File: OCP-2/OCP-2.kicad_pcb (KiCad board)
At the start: 2 copper layers, 100 x 100 mm, 139 parts, among them X1 ico*отверстие*М3, X2 ico*отверстие*М3

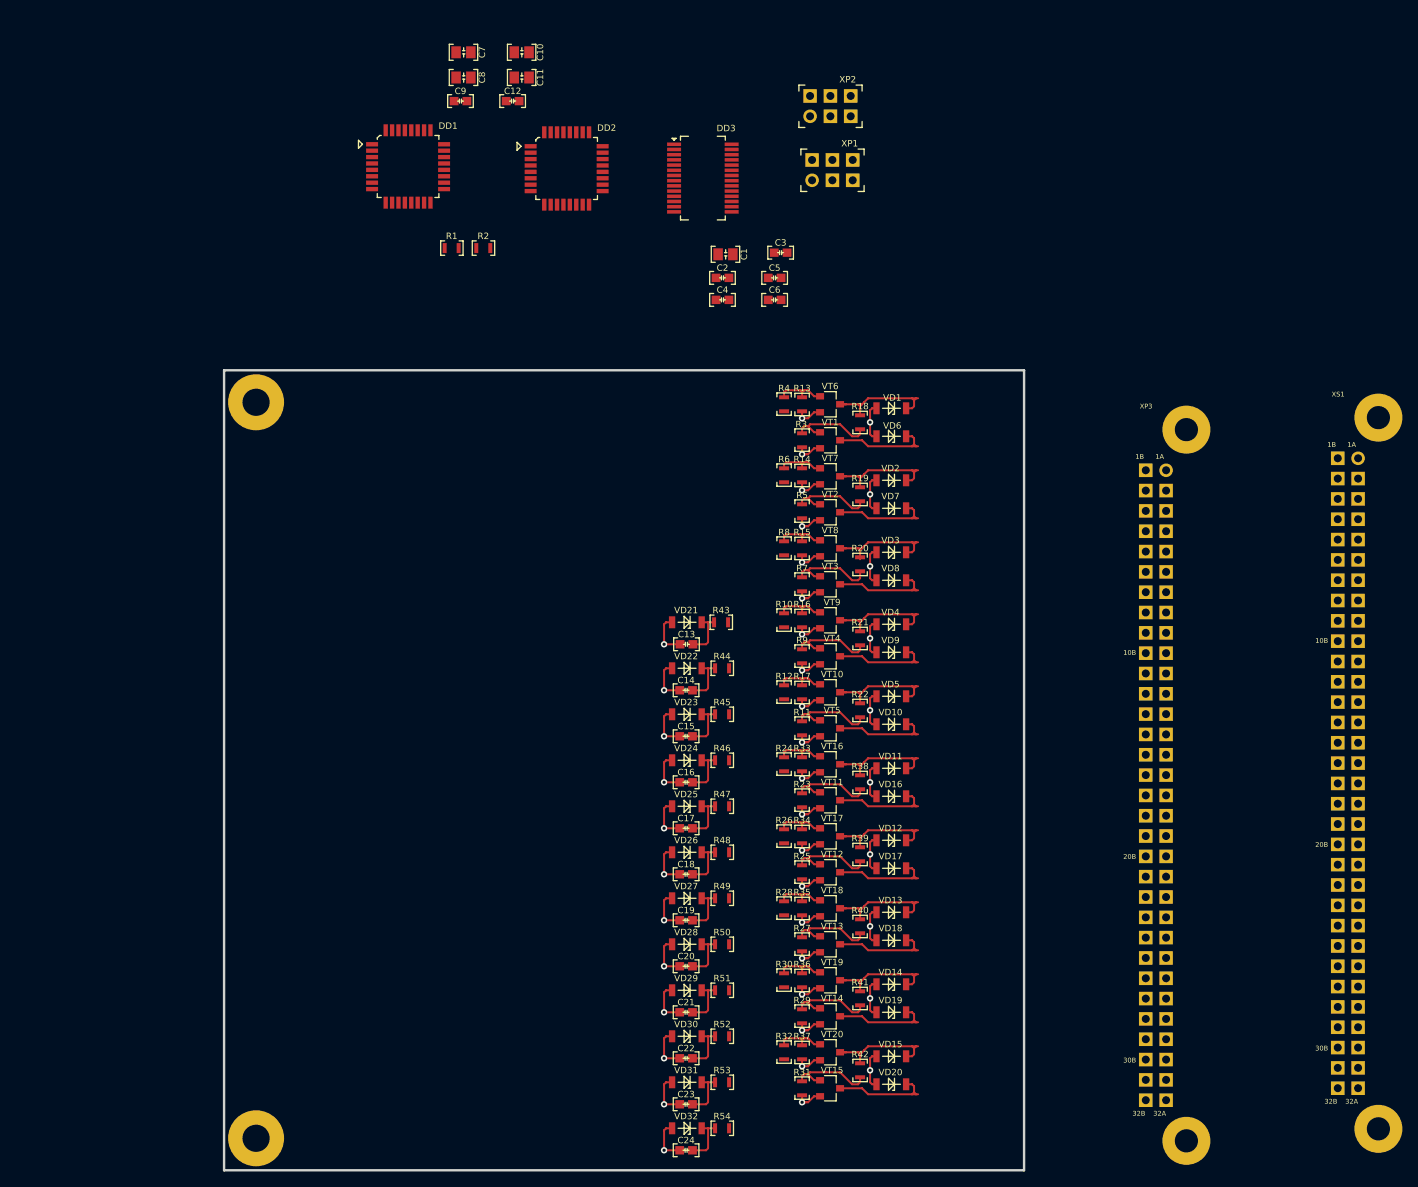
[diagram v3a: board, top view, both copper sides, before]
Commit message: размещена схема DI, схема не подбита
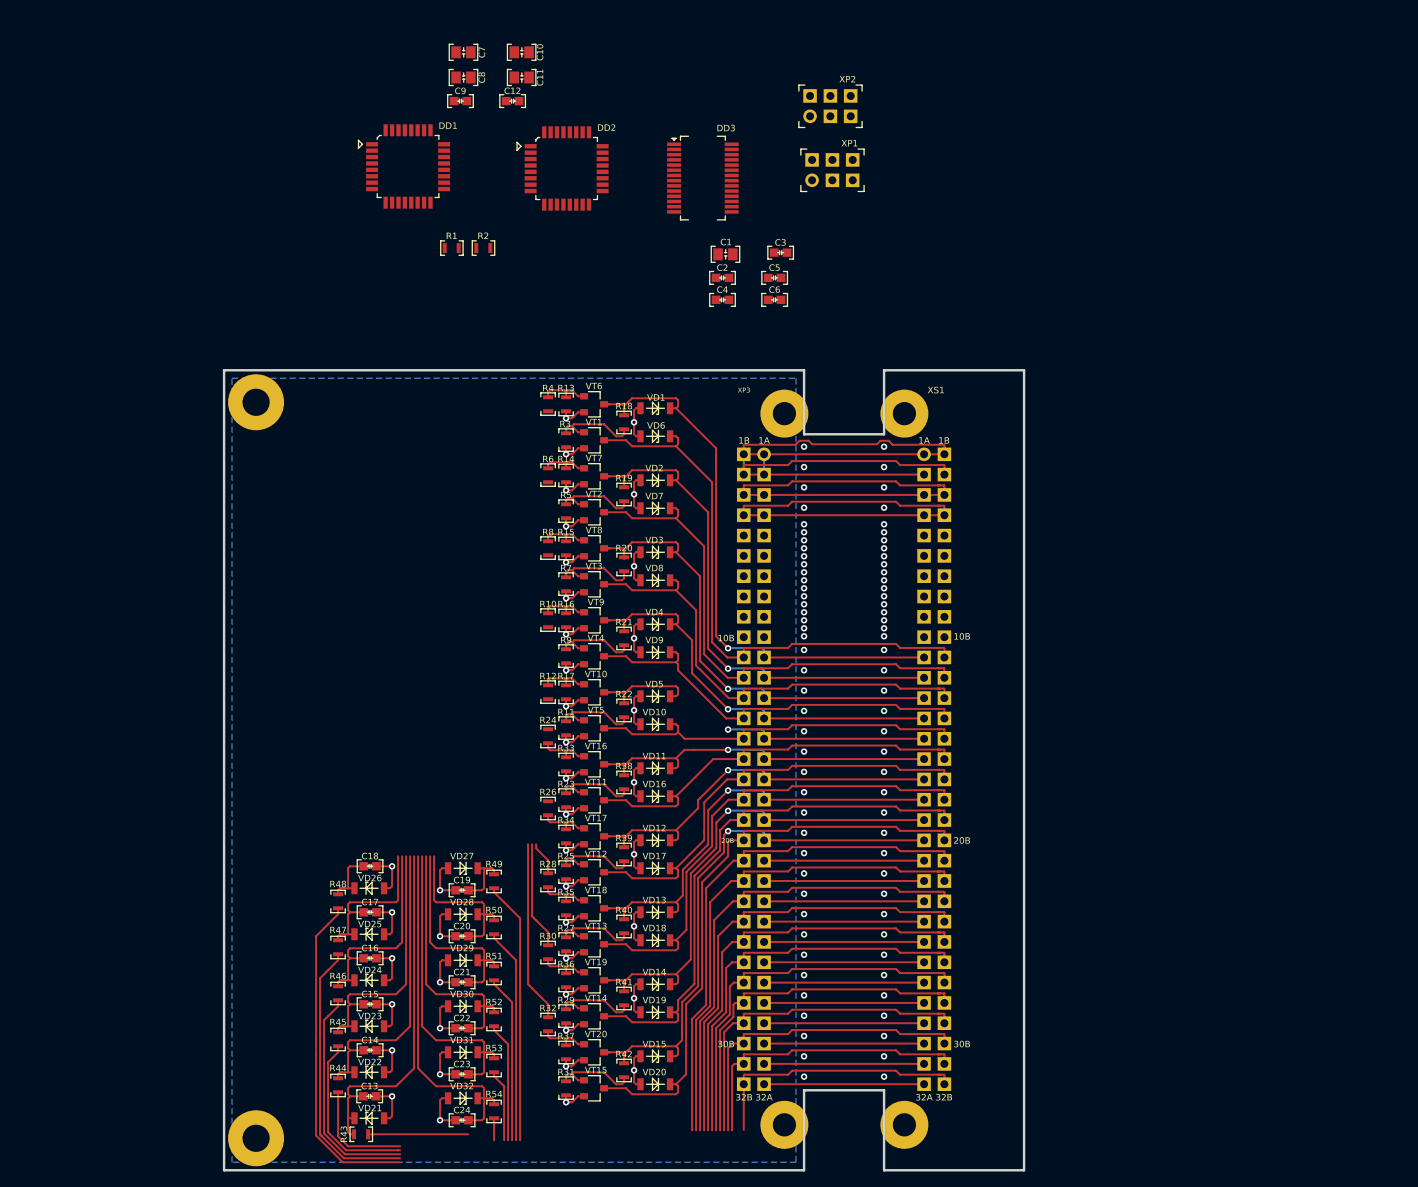
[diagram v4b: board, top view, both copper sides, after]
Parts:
- moved R43 78.2 mm to (67.1, 145.5)
- moved VD21 71.7 mm to (70.0, 143.5), turned to 180 degrees
- moved R44 70.9 mm to (64.2, 139.4), turned to 270 degrees
- moved C13 69.0 mm to (68.2, 140.8), turned to 180 degrees
- moved R45 62.9 mm to (64.2, 133.6), turned to 270 degrees
- moved VD22 62.0 mm to (70.0, 137.8), turned to 180 degrees
- moved C14 59.9 mm to (68.2, 135.0), turned to 180 degrees
- moved R46 56.1 mm to (64.2, 127.9), turned to 270 degrees
- moved XS1 54.3 mm to (137.5, 60.5)
- moved VD23 53.1 mm to (70.0, 132.0), turned to 180 degrees
- moved C15 51.8 mm to (68.2, 129.2), turned to 180 degrees
- moved R47 51.1 mm to (64.2, 122.1), turned to 270 degrees
- moved XP3 50.3 mm to (117.5, 60.5)
- moved R48 48.4 mm to (64.2, 116.4), turned to 270 degrees
- moved VD24 45.3 mm to (70.0, 126.2), turned to 180 degrees
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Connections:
- VD10 pad 2: /DOU5.PNP -> /DOUT5.PNP
- VD20 pad 2: /DOU10.PNP -> /DOUT10.PNP
- VT15 pad 3: /DOU10.PNP -> /DOUT10.PNP
- VT5 pad 3: /DOU5.PNP -> /DOUT5.PNP
- XP3 pad 11A: Net-(XP3-Pad11A) -> /DOUT1.NPN
- XP3 pad 11B: Net-(XP3-Pad11B) -> /DOUT1.PNP
- XP3 pad 12A: Net-(XP3-Pad12A) -> /DOUT2.NPN
- XP3 pad 12B: Net-(XP3-Pad12B) -> /DOUT2.PNP
- XP3 pad 13A: Net-(XP3-Pad13A) -> /DOUT3.NPN
- XP3 pad 13B: Net-(XP3-Pad13B) -> /DOUT3.PNP
- XP3 pad 14A: Net-(XP3-Pad14A) -> /DOUT4.NPN
- XP3 pad 14B: Net-(XP3-Pad14B) -> /DOUT4.PNP
- XP3 pad 15A: Net-(XP3-Pad15A) -> /DOUT5.NPN
- XP3 pad 15B: Net-(XP3-Pad15B) -> /DOUT5.PNP
- XP3 pad 16A: Net-(XP3-Pad16A) -> /DOUT6.NPN
- XP3 pad 16B: Net-(XP3-Pad16B) -> /DOUT6.PNP
- XP3 pad 17A: Net-(XP3-Pad17A) -> /DOUT7.NPN
- XP3 pad 17B: Net-(XP3-Pad17B) -> /DOUT7.PNP
- XP3 pad 18A: Net-(XP3-Pad18A) -> /DOUT8.NPN
- XP3 pad 18B: Net-(XP3-Pad18B) -> /DOUT8.PNP
- XP3 pad 19A: Net-(XP3-Pad19A) -> /DOUT9.NPN
- XP3 pad 19B: Net-(XP3-Pad19B) -> /DOUT9.PNP
- XP3 pad 1A: Net-(XP3-Pad1A) -> 5V
- XP3 pad 1B: Net-(XP3-Pad1B) -> 5V
- XP3 pad 20A: Net-(XP3-Pad20A) -> /DOUT10.NPN
- XP3 pad 20B: Net-(XP3-Pad20B) -> /DOUT10.PNP
- XP3 pad 21A: Net-(XP3-Pad21A) -> /RESERVE1
- XP3 pad 21B: Net-(XP3-Pad21B) -> /DIN1
- XP3 pad 22A: Net-(XP3-Pad22A) -> /RESERVE2
- XP3 pad 22B: Net-(XP3-Pad22B) -> /DIN2
- XP3 pad 23A: Net-(XP3-Pad23A) -> /RESERVE3
- XP3 pad 23B: Net-(XP3-Pad23B) -> /DIN3
- XP3 pad 24A: Net-(XP3-Pad24A) -> /RESERVE4
- XP3 pad 24B: Net-(XP3-Pad24B) -> /DIN4
- XP3 pad 25A: Net-(XP3-Pad25A) -> /RESERVE5
- XP3 pad 25B: Net-(XP3-Pad25B) -> /DIN5
- XP3 pad 26A: Net-(XP3-Pad26A) -> /RESERVE6
- XP3 pad 26B: Net-(XP3-Pad26B) -> /DIN6
- XP3 pad 27A: Net-(XP3-Pad27A) -> /RESERVE7
- XP3 pad 27B: Net-(XP3-Pad27B) -> /DIN7
- XP3 pad 28A: Net-(XP3-Pad28A) -> /RESERVE8
- XP3 pad 28B: Net-(XP3-Pad28B) -> /DIN8
- XP3 pad 29A: Net-(XP3-Pad29A) -> /RESERVE9
- XP3 pad 29B: Net-(XP3-Pad29B) -> /DIN9
- XP3 pad 2A: Net-(XP3-Pad2A) -> 5V
- XP3 pad 2B: Net-(XP3-Pad2B) -> 5V
- XP3 pad 30A: Net-(XP3-Pad30A) -> /RESERVE10
- XP3 pad 30B: Net-(XP3-Pad30B) -> /DIN10
- XP3 pad 31A: Net-(XP3-Pad31A) -> /RESERVE11
- XP3 pad 31B: Net-(XP3-Pad31B) -> /DIN11
- XP3 pad 32A: Net-(XP3-Pad32A) -> /RESERVE12
- XP3 pad 32B: Net-(XP3-Pad32B) -> /DIN12
- XP3 pad 3A: Net-(XP3-Pad3A) -> GND
- XP3 pad 3B: Net-(XP3-Pad3B) -> GND
- XP3 pad 4A: Net-(XP3-Pad4A) -> GND
- XP3 pad 4B: Net-(XP3-Pad4B) -> GND
- XS1 pad 11A: Net-(XS1-Pad11A) -> /DOUT1.NPN
- XS1 pad 11B: Net-(XS1-Pad11B) -> /DOUT1.PNP
- XS1 pad 12A: Net-(XS1-Pad12A) -> /DOUT2.NPN
- XS1 pad 12B: Net-(XS1-Pad12B) -> /DOUT2.PNP
- XS1 pad 13A: Net-(XS1-Pad13A) -> /DOUT3.NPN
- XS1 pad 13B: Net-(XS1-Pad13B) -> /DOUT3.PNP
- XS1 pad 14A: Net-(XS1-Pad14A) -> /DOUT4.NPN
- XS1 pad 14B: Net-(XS1-Pad14B) -> /DOUT4.PNP
- XS1 pad 15A: Net-(XS1-Pad15A) -> /DOUT5.NPN
- XS1 pad 15B: Net-(XS1-Pad15B) -> /DOUT5.PNP
- XS1 pad 16A: Net-(XS1-Pad16A) -> /DOUT6.NPN
- XS1 pad 16B: Net-(XS1-Pad16B) -> /DOUT6.PNP
- XS1 pad 17A: Net-(XS1-Pad17A) -> /DOUT7.NPN
- XS1 pad 17B: Net-(XS1-Pad17B) -> /DOUT7.PNP
- XS1 pad 18A: Net-(XS1-Pad18A) -> /DOUT8.NPN
- XS1 pad 18B: Net-(XS1-Pad18B) -> /DOUT8.PNP
- XS1 pad 19A: Net-(XS1-Pad19A) -> /DOUT9.NPN
- XS1 pad 19B: Net-(XS1-Pad19B) -> /DOUT9.PNP
- XS1 pad 1A: Net-(XS1-Pad1A) -> 5V
- XS1 pad 1B: Net-(XS1-Pad1B) -> 5V
- XS1 pad 20A: Net-(XS1-Pad20A) -> /DOUT10.NPN
- XS1 pad 20B: Net-(XS1-Pad20B) -> /DOUT10.PNP
- XS1 pad 21A: Net-(XS1-Pad21A) -> /RESERVE1
- XS1 pad 21B: Net-(XS1-Pad21B) -> /DIN1
- XS1 pad 22A: Net-(XS1-Pad22A) -> /RESERVE2
- XS1 pad 22B: Net-(XS1-Pad22B) -> /DIN2
- XS1 pad 23A: Net-(XS1-Pad23A) -> /RESERVE3
- XS1 pad 23B: Net-(XS1-Pad23B) -> /DIN3
- XS1 pad 24A: Net-(XS1-Pad24A) -> /RESERVE4
- XS1 pad 24B: Net-(XS1-Pad24B) -> /DIN4
- XS1 pad 25A: Net-(XS1-Pad25A) -> /RESERVE5
- XS1 pad 25B: Net-(XS1-Pad25B) -> /DIN5
- XS1 pad 26A: Net-(XS1-Pad26A) -> /RESERVE6
- XS1 pad 26B: Net-(XS1-Pad26B) -> /DIN6
- XS1 pad 27A: Net-(XS1-Pad27A) -> /RESERVE7
- XS1 pad 27B: Net-(XS1-Pad27B) -> /DIN7
- XS1 pad 28A: Net-(XS1-Pad28A) -> /RESERVE8
- XS1 pad 28B: Net-(XS1-Pad28B) -> /DIN8
- XS1 pad 29A: Net-(XS1-Pad29A) -> /RESERVE9
- XS1 pad 29B: Net-(XS1-Pad29B) -> /DIN9
- XS1 pad 2A: Net-(XS1-Pad2A) -> 5V
- XS1 pad 2B: Net-(XS1-Pad2B) -> 5V
- XS1 pad 30A: Net-(XS1-Pad30A) -> /RESERVE10
- XS1 pad 30B: Net-(XS1-Pad30B) -> /DIN10
- XS1 pad 31A: Net-(XS1-Pad31A) -> /RESERVE11
- XS1 pad 31B: Net-(XS1-Pad31B) -> /DIN11
- XS1 pad 32A: Net-(XS1-Pad32A) -> /RESERVE12
- XS1 pad 32B: Net-(XS1-Pad32B) -> /DIN12
- XS1 pad 3A: Net-(XS1-Pad3A) -> GND
- XS1 pad 3B: Net-(XS1-Pad3B) -> GND
- XS1 pad 4A: Net-(XS1-Pad4A) -> GND
- XS1 pad 4B: Net-(XS1-Pad4B) -> GND
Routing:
- net 5V: track 39.4 -> 148.6 mm
- net GND: track 149.3 -> 255.6 mm
- net /DIN6: track 0.00 -> 93.0 mm
- net /DIN5: track 0.00 -> 89.5 mm
- net /DIN4: track 0.00 -> 85.0 mm
- net /DIN7: track 0.00 -> 81.5 mm
- net /DIN3: track 0.00 -> 80.9 mm
- net /DIN1: track 0.00 -> 77.7 mm
- net /DIN2: track 0.00 -> 76.4 mm
- net /DOUT10.PNP: track 0.00 -> 74.6 mm
- net /DIN8: track 0.00 -> 72.7 mm
- net /DIN9: track 0.00 -> 64.2 mm
- net /DOUT1.NPN: track 14.7 -> 73.8 mm, vias 0 -> 1
- net /DOUT1.PNP: track 12.6 -> 70.7 mm
- net /DIN10: track 0.00 -> 55.5 mm
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- added copper zone on B.Cu, net GND
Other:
- outline, holes or cut-outs redrawn

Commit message: изменена вилка программирования, вынесена розетка ETH
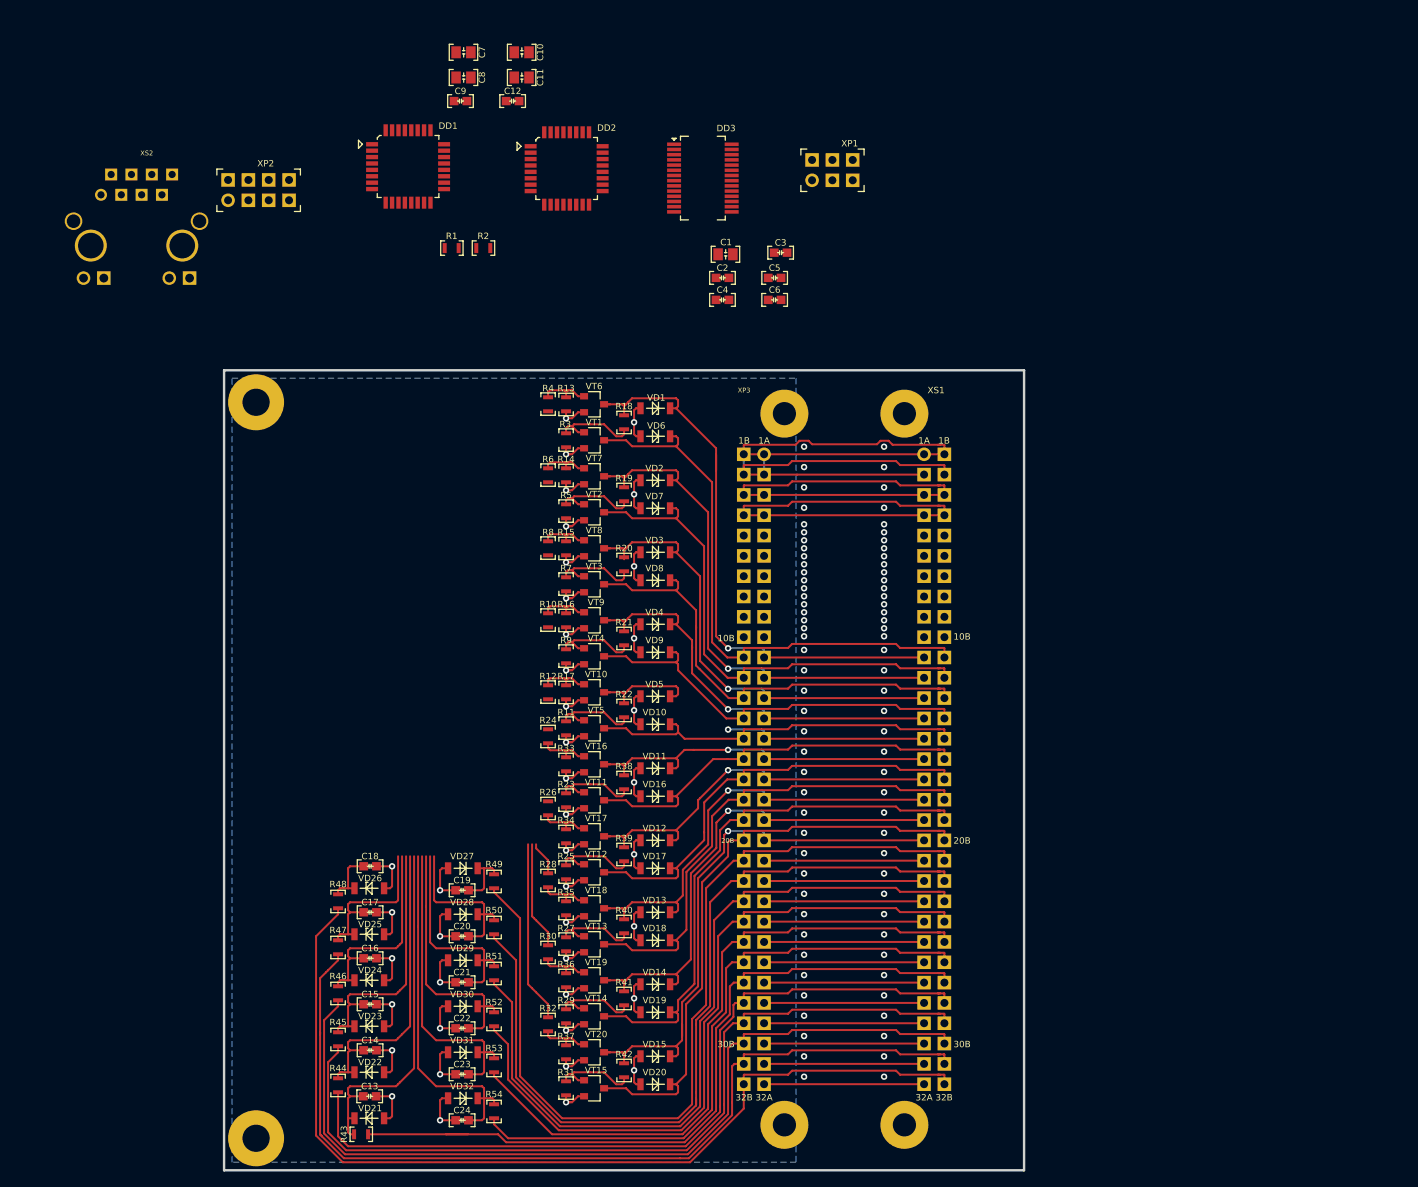
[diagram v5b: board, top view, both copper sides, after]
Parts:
- added XS2: Розетка*ETH+трансформатор*8p8c, N_X:Розетка_ETH_KLS12-TL002, F.Cu at (34.6, 28.1)
- XP2: value Вилка*PLD*6контактов*2ряда*вертикальная*AVR -> Вилка*PLD*8контактов*2ряда*вертикальная*AVR+UART; footprint N_X:Вилка_PLD6_вертикальная_AB -> N_X:Вилка_PLD8_вертикальная_AB
- moved XP2 73.5 mm to (50.5, 28.8)
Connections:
- DD1 pad 30: Net-(DD1-Pad30) -> /RX
- DD1 pad 31: Net-(DD1-Pad31) -> /TX
- XP3 pad 21B: /DIN1 -> /DIN7
- XP3 pad 22B: /DIN2 -> /DIN8
- XP3 pad 23B: /DIN3 -> /DIN9
- XP3 pad 24B: /DIN4 -> /DIN10
- XP3 pad 25B: /DIN5 -> /DIN11
- XP3 pad 26B: /DIN6 -> /DIN12
- XP3 pad 27B: /DIN7 -> /DIN1
- XP3 pad 28B: /DIN8 -> /DIN2
- XP3 pad 29B: /DIN9 -> /DIN3
- XP3 pad 30B: /DIN10 -> /DIN4
- XP3 pad 31B: /DIN11 -> /DIN5
- XP3 pad 32B: /DIN12 -> /DIN6
- XS1 pad 21B: /DIN1 -> /DIN7
- XS1 pad 22B: /DIN2 -> /DIN8
- XS1 pad 23B: /DIN3 -> /DIN9
- XS1 pad 24B: /DIN4 -> /DIN10
- XS1 pad 25B: /DIN5 -> /DIN11
- XS1 pad 26B: /DIN6 -> /DIN12
- XS1 pad 27B: /DIN7 -> /DIN1
- XS1 pad 28B: /DIN8 -> /DIN2
- XS1 pad 29B: /DIN9 -> /DIN3
- XS1 pad 30B: /DIN10 -> /DIN4
- XS1 pad 31B: /DIN11 -> /DIN5
- XS1 pad 32B: /DIN12 -> /DIN6
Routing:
- net /DIN12: track 36.5 -> 79.2 mm
- net /DIN11: track 46.7 -> 83.2 mm
- net /DIN10: track 55.5 -> 89.9 mm
- net /DIN9: track 64.2 -> 97.0 mm
- net /DIN8: track 72.7 -> 105.1 mm
- net /DIN7: track 81.5 -> 111.2 mm
- net /DIN6: track 93.0 -> 118.3 mm
- net /DIN5: track 89.5 -> 114.7 mm
- net /DIN4: track 85.0 -> 109.5 mm
- net /DIN3: track 80.9 -> 104.7 mm
- net /DIN2: track 76.4 -> 99.1 mm
- net /DIN1: track 77.7 -> 94.6 mm
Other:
- outline, holes or cut-outs redrawn
